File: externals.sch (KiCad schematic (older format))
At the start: 40 parts, among them J1 Micro_SD, J2 RC522_Header, J3 Screw_Terminal_1x02, P1 SWD, P2 VolDown, P3 Prev, P4 Play, P5 Next, P6 VolUp, P7 CONN_02X10, Q1 BSS138

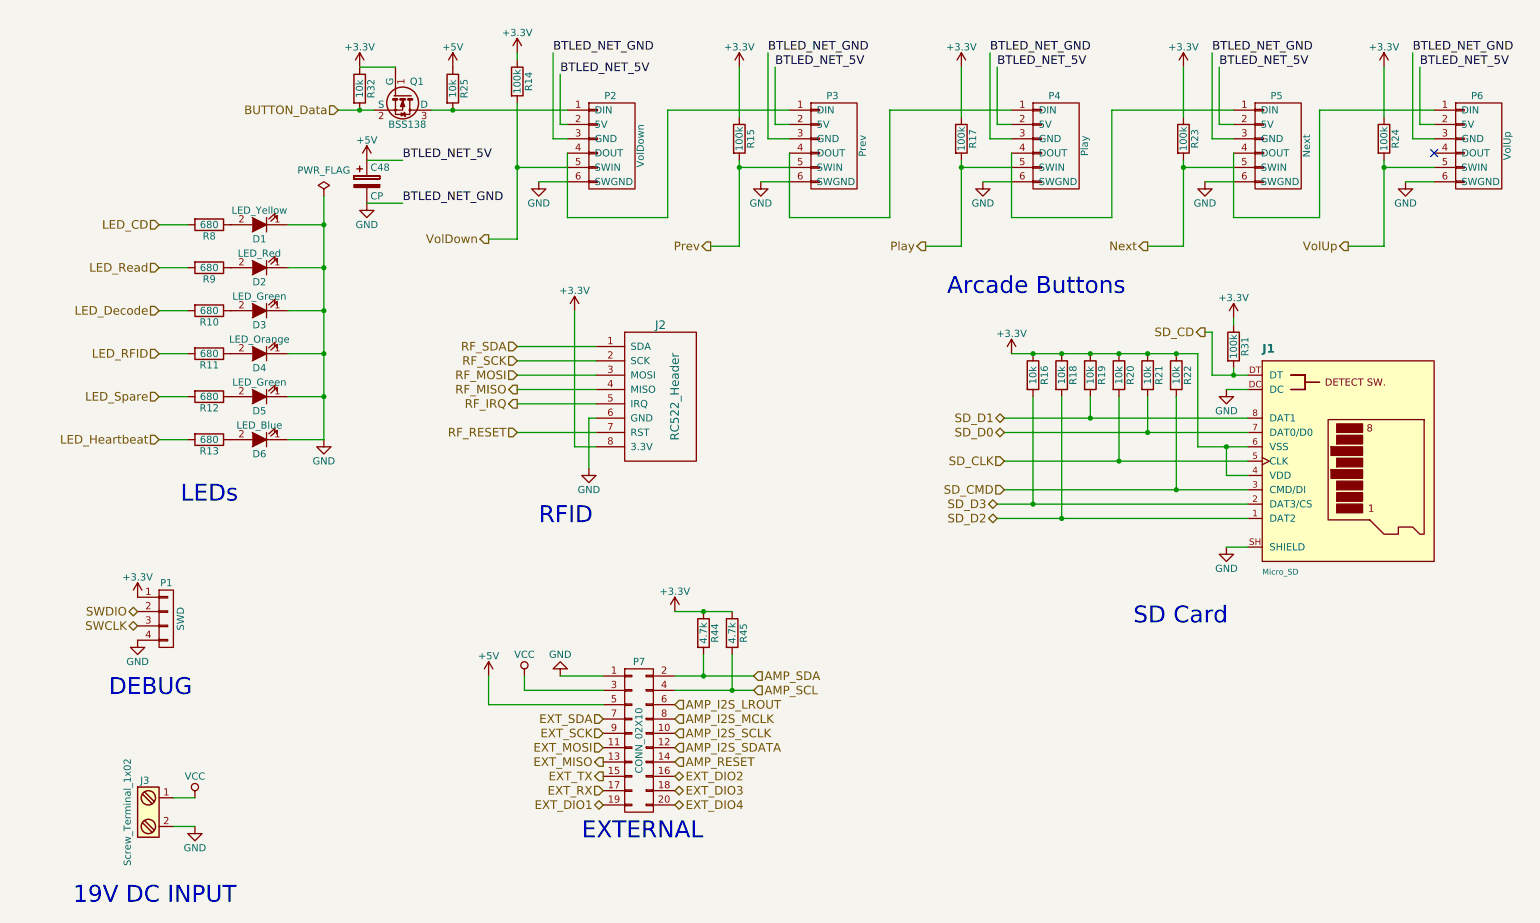
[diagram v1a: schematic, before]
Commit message: Use smd oscilator Add testpoints Use different power networks
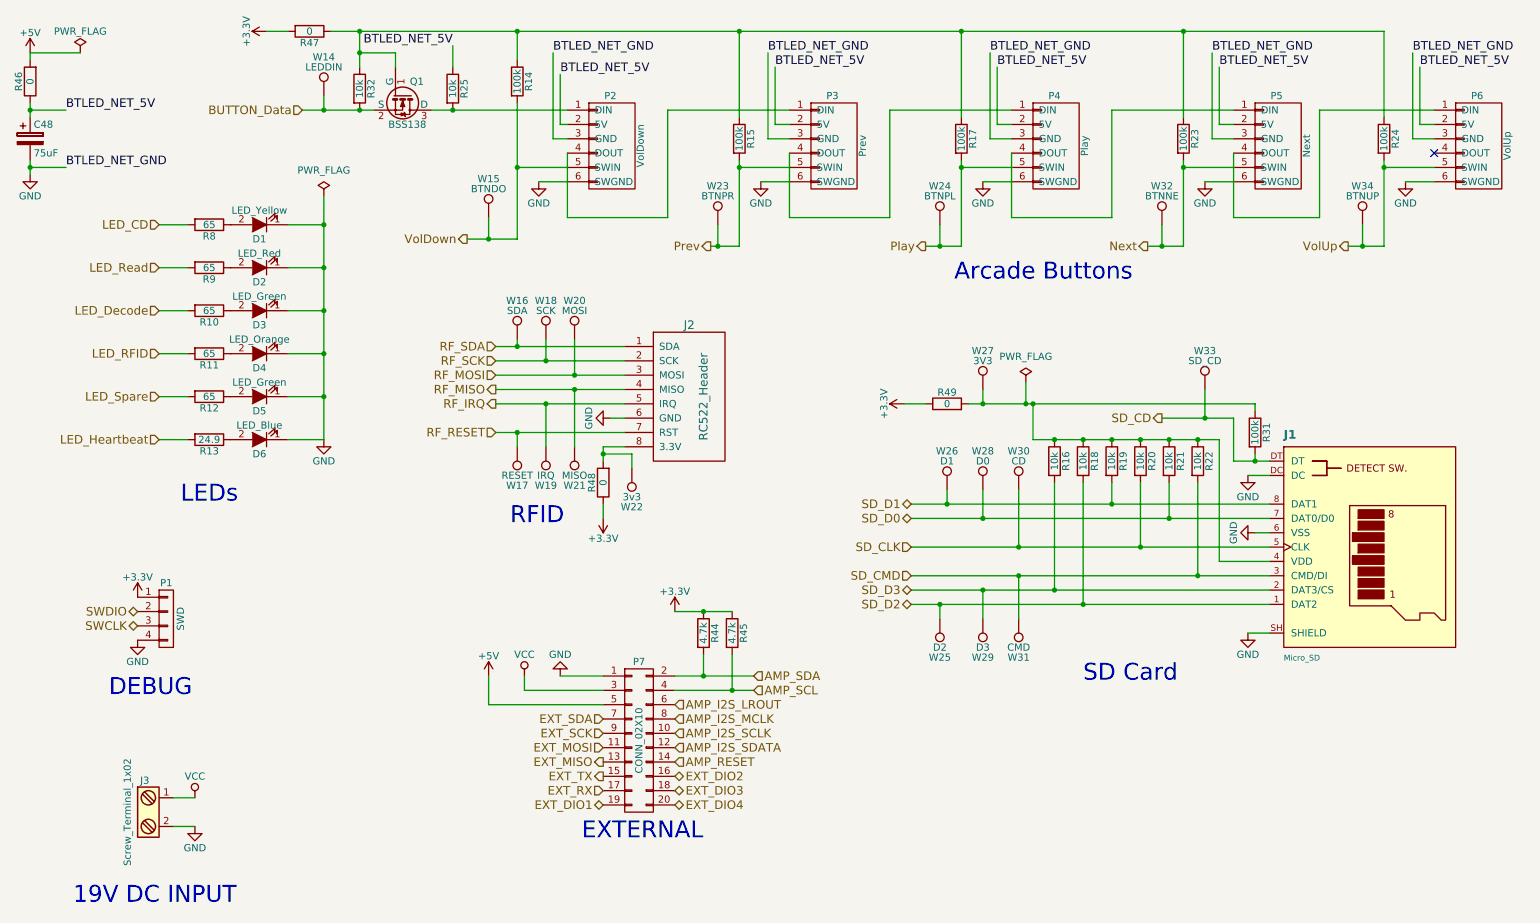
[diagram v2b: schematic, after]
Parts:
- added R46, R47: 0, Resistors_SMD:R_0603_HandSoldering, symbol R
- added R48, R49: 0, Resistors_SMD:R_0603, symbol R
- added W14: LEDDIN, Measurement_Points:Measurement_Point_Round-SMD-Pad_Small, symbol TEST_1P
- added W15: BTNDO, Measurement_Points:Measurement_Point_Round-SMD-Pad_Small, symbol TEST_1P
- added W16: SDA, Measurement_Points:Measurement_Point_Round-SMD-Pad_Small, symbol TEST_1P
- added W17: RESET, Measurement_Points:Measurement_Point_Round-SMD-Pad_Small, symbol TEST_1P
- added W18: SCK, Measurement_Points:Measurement_Point_Round-SMD-Pad_Small, symbol TEST_1P
- added W19: IRQ, Measurement_Points:Measurement_Point_Round-SMD-Pad_Small, symbol TEST_1P
- added W20: MOSI, Measurement_Points:Measurement_Point_Round-SMD-Pad_Small, symbol TEST_1P
- added W21: MISO, Measurement_Points:Measurement_Point_Round-SMD-Pad_Small, symbol TEST_1P
- added W22: 3v3, Measurement_Points:Measurement_Point_Round-SMD-Pad_Small, symbol TEST_1P
- added W23: BTNPR, Measurement_Points:Measurement_Point_Round-SMD-Pad_Small, symbol TEST_1P
- added W24: BTNPL, Measurement_Points:Measurement_Point_Round-SMD-Pad_Small, symbol TEST_1P
- added W25: D2, Measurement_Points:Measurement_Point_Round-SMD-Pad_Small, symbol TEST_1P
- added W26: D1, Measurement_Points:Measurement_Point_Round-SMD-Pad_Small, symbol TEST_1P
- added W27: 3V3, Measurement_Points:Measurement_Point_Round-SMD-Pad_Small, symbol TEST_1P
- added W28: D0, Measurement_Points:Measurement_Point_Round-SMD-Pad_Small, symbol TEST_1P
- added W29: D3, Measurement_Points:Measurement_Point_Round-SMD-Pad_Small, symbol TEST_1P
- added W30: CD, Measurement_Points:Measurement_Point_Round-SMD-Pad_Small, symbol TEST_1P
- added W31: CMD, Measurement_Points:Measurement_Point_Round-SMD-Pad_Small, symbol TEST_1P
- added W32: BTNNE, Measurement_Points:Measurement_Point_Round-SMD-Pad_Small, symbol TEST_1P
- added W33: SD_CD, Measurement_Points:Measurement_Point_Round-SMD-Pad_Small, symbol TEST_1P
- added W34: BTNUP, Measurement_Points:Measurement_Point_Round-SMD-Pad_Small, symbol TEST_1P
- C48: value CP -> 75uF; footprint Capacitors_THT:C_Radial_D5_L6_P2.5 -> Capacitors_SMD:c_elec_5x5.7
- R10, R11, R12, R8, R9: value 680 -> 65; MPN RC0603JR-07680RL -> RC0201FR-0764R9L; SPN 603-RC0603JR-07680RL -> 603-RC0201FR-0764R9L
- R13: value 680 -> 24.9; MPN RC0603JR-07680RL -> RC0201FR-0724R9L; SPN 603-RC0603JR-07680RL -> 603-RC0201FR-0724R9L
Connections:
- net +3V3: now also R47.2, R48.1, R49.1; no longer J1.4 (VDD), J1.6 (VSS), J2.8 (3.3V), Q1.1 (G), R14.1, R15.1, R16.1, R17.1, R18.1, R19.1, R20.1, R21.1, R22.1, R23.1, R24.1, R31.1, R32.1
- net +5V: now also R46.2; no longer C48.1, P2.2 (5V), P3.2 (5V), P4.2 (5V), P5.2 (5V), P6.2 (5V), R25.1
- net BUTTON_Data: now also W14.1
- net GND: now also J1.6 (VSS)
- net Next: now also W32.1
- net Play: now also W24.1
- net Prev: now also W23.1
- net RF_IRQ: now also W19.1
- net RF_MISO: now also W21.1
- net RF_MOSI: now also W20.1
- net RF_RESET: now also W17.1
- net RF_SCK: now also W18.1
- net RF_SDA: now also W16.1
- net SD_CD: now also W33.1
- net SD_CLK: now also W30.1
- net SD_CMD: now also W31.1
- net SD_D0: now also W28.1
- net SD_D1: now also W26.1
- net SD_D2: now also W25.1
- net SD_D3: now also W29.1
- net VolDown: now also W15.1
- net VolUp: now also W34.1
- new net: Q1.1 (G), R14.1, R15.1, R17.1, R23.1, R24.1, R32.1, R47.1
- new net: J1.4 (VDD), R16.1, R18.1, R19.1, R20.1, R21.1, R22.1, R31.1, R49.2, W27.1
- new net: J2.8 (3.3V), R48.2, W22.1
- new net BTLED_NET_5V: C48.1, P2.2 (5V), P3.2 (5V), P4.2 (5V), P5.2 (5V), P6.2 (5V), R25.1, R46.1
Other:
- moved on the sheet: C48, J1, J2, R16, R18, R19, R20, R21, R22, R31

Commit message: new layout
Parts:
- D1, D2, D3, D4, D5, D6: footprint Capacitors_SMD:C_0603_HandSoldering -> Diodes_SMD:D_0603
- R10, R11, R12, R8, R9: value 65 -> 680; footprint Resistors_SMD:R_0603_HandSoldering -> Resistors_SMD:R_0603; MPN RC0201FR-0764R9L -> RC0603JR-07680RL; SPN 603-RC0201FR-0764R9L -> 603-RC0603JR-07680RL
- R13: value 24.9 -> 680; footprint Resistors_SMD:R_0603_HandSoldering -> Resistors_SMD:R_0603; MPN RC0201FR-0724R9L -> RC0603JR-07680RL; SPN 603-RC0201FR-0724R9L -> 603-RC0603JR-07680RL
- R14, R15, R16, R17, R18, R19, R20, R21, R22, R23, R24, R25, R31, R32, R44, R45, R46, R47: footprint Resistors_SMD:R_0603_HandSoldering -> Resistors_SMD:R_0603

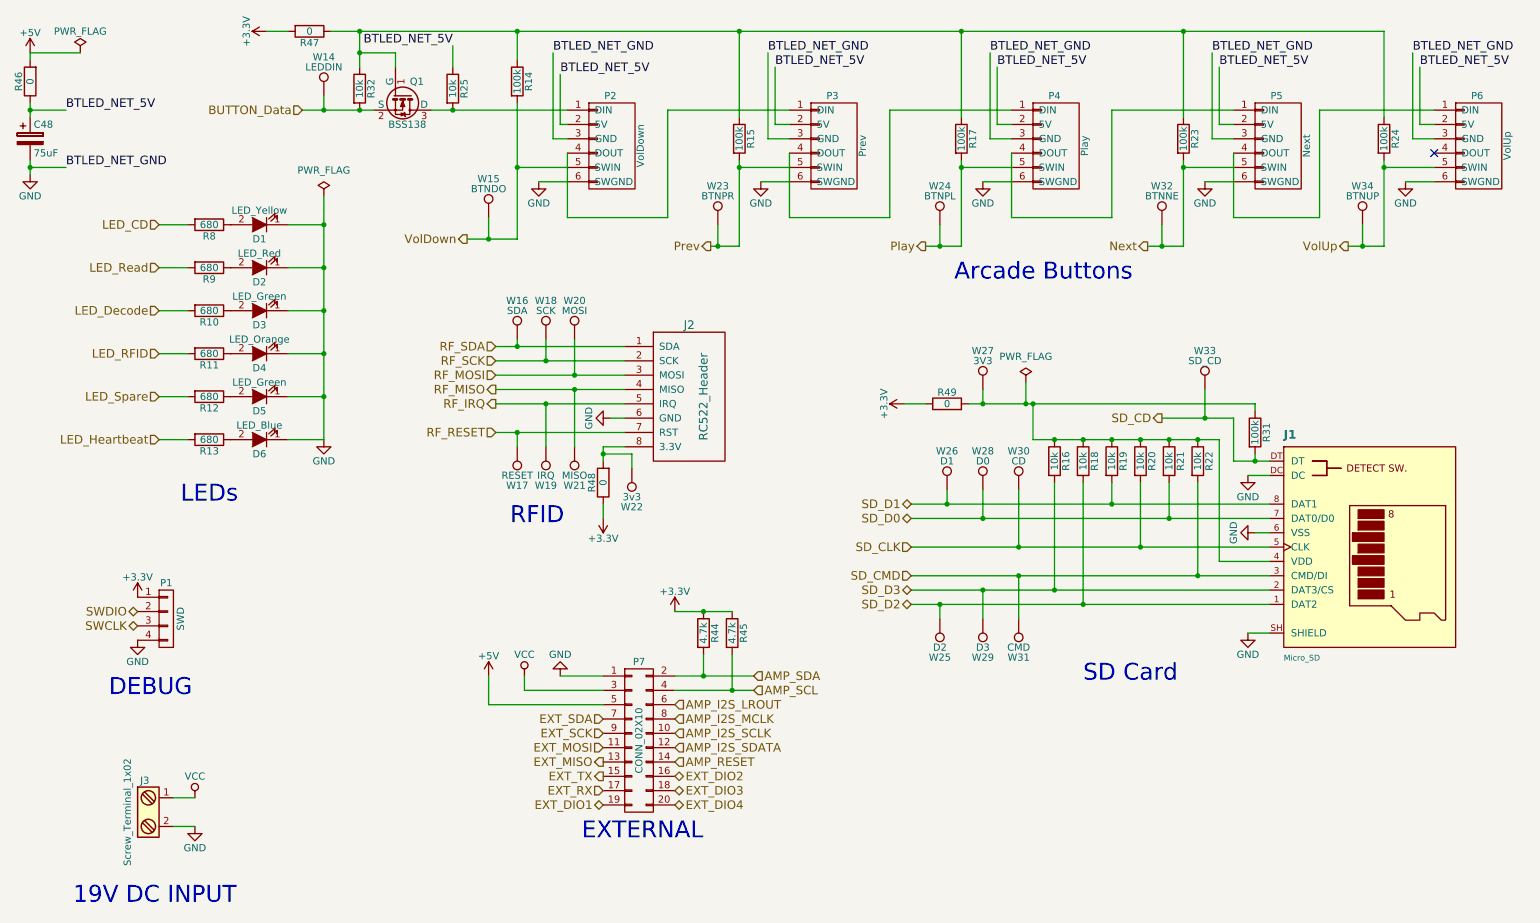
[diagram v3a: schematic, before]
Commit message: Macrofab sd card footprint
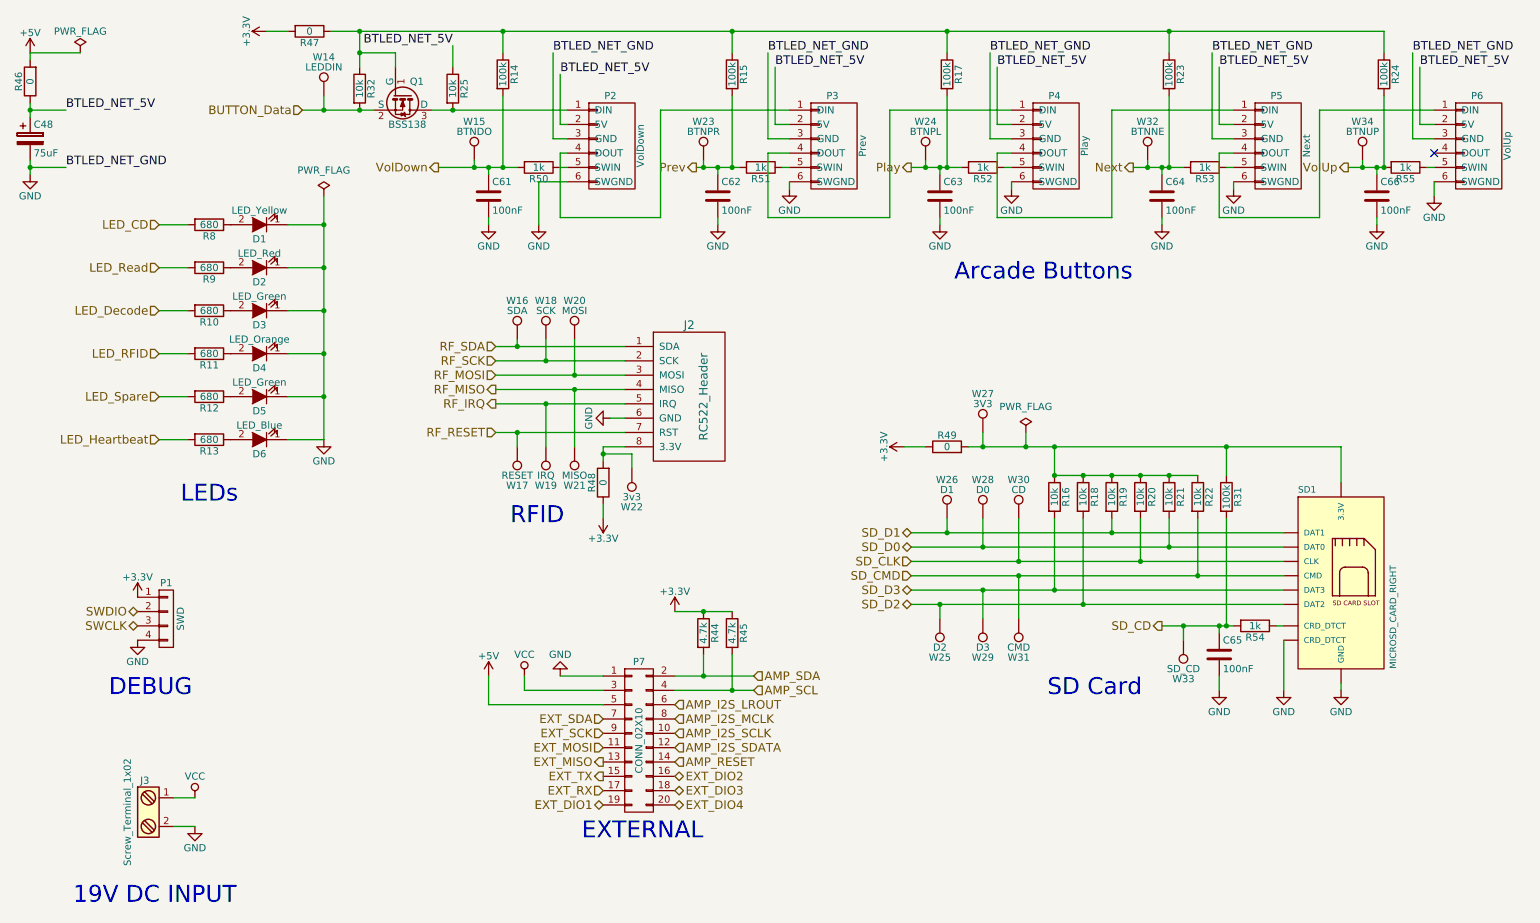
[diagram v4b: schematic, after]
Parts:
- removed J1: Micro_SD, conn-io:HIROSE-MICROSD-DM3AT-SF, symbol Micro_SD
- added C61, C62, C63, C64, C65, C66: 100nF, Capacitors_SMD:C_0402, symbol C
- added R50, R51, R52, R53, R54, R55: 1k, Resistors_SMD:R_0603, symbol R
- added SD1: MICROSD_CARD_RIGHT, MF_Connectors_MF-MICROSD, symbol MICROSD_CARD_RIGHT
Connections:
- net GND: now also C61.2, C62.2, C63.2, C64.2, C65.2, C66.2, SD1.10 (CRD_DTCT), SD1.6 (GND), SD1.G0 (GND), SD1.G1 (GND)
- net Next: now also C64.1, R53.2; no longer P5.5 (SWIN)
- net Play: now also C63.1, R52.2; no longer P4.5 (SWIN)
- net Prev: now also C62.1, R51.2; no longer P3.5 (SWIN)
- net SD_CD: now also C65.1, R54.2
- net SD_CLK: now also SD1.5 (CLK)
- net SD_CMD: now also SD1.3 (CMD)
- net SD_D0: now also SD1.7 (DAT0)
- net SD_D1: now also SD1.8 (DAT1)
- net SD_D2: now also SD1.1 (DAT2)
- net SD_D3: now also SD1.2 (DAT3)
- net VolDown: now also C61.1, R50.2; no longer P2.5 (SWIN)
- net VolUp: now also C66.1, R55.2; no longer P6.5 (SWIN)
- net at R16.1, R18.1, R19.1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: now also SD1.4 (3.3V)
- new net: P2.5 (SWIN), R50.1
- new net: P3.5 (SWIN), R51.1
- new net: P4.5 (SWIN), R52.1
- new net: P5.5 (SWIN), R53.1
- new net: P6.5 (SWIN), R55.1
- new net: R54.1, SD1.9 (CRD_DTCT)
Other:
- moved on the sheet: R14, R15, R16, R17, R18, R19, R20, R21, R22, R23, R24, R31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

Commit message: Finished new layout
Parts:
- C48: MFR (none) -> Panasonic; MPN (none) -> EEE-HD1V100AR; SPN (none) -> 667-EEE-HD1V100AR; SPR (none) -> Mouser
- C61, C62, C63, C64, C65, C66: MFR (none) -> KEMET; MPN (none) -> C0402C104M4RACAUTO; SPN (none) -> 80-C0402C104M4RAUTO; SPR (none) -> Mouser
- R46, R47: MPN RC0603JR-07100KL -> RC0603JR-070RL; SPN 603-RC0603JR-07100KL -> 603-RC0603JR-070RL
- SD1: MFR (none) -> Molex; MPN (none) -> 47334-0001; SPN (none) -> 538-47334-0001; SPR (none) -> Mouser
- W22: value 3v3 -> 3V3

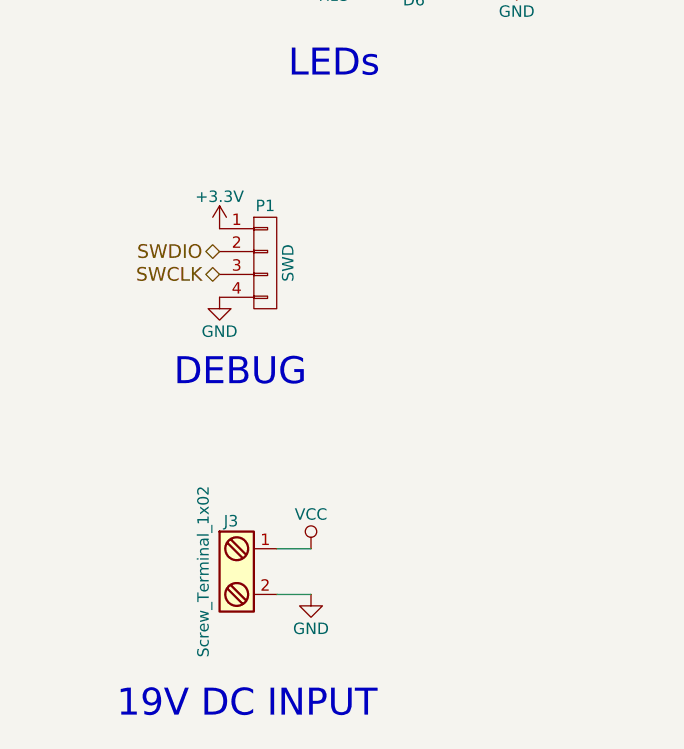
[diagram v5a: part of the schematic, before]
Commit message: Remove 3. LDO some improvements
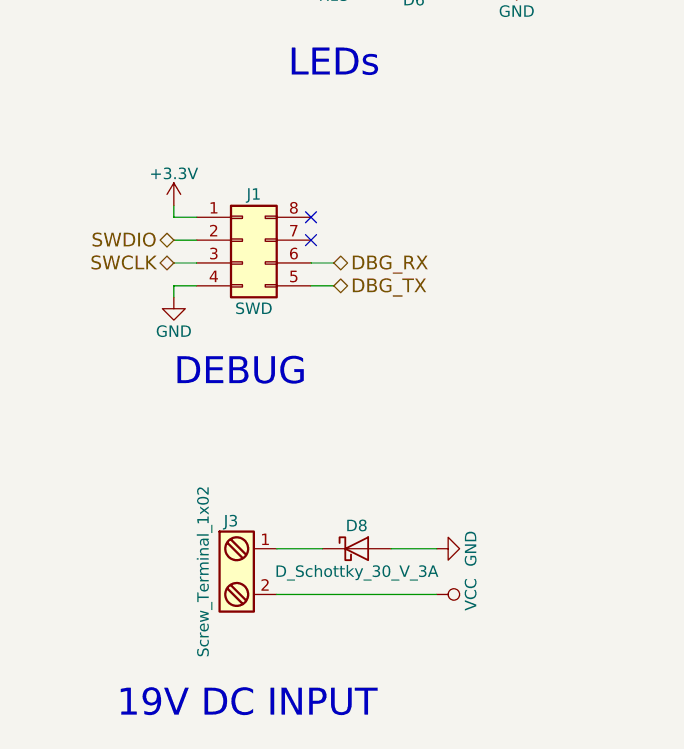
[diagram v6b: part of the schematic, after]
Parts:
- removed P1: SWD, Pin_Headers:Pin_Header_Straight_1x04, symbol CONN_01X04
- added D8: D_Schottky_30_V_3A, Diodes_SMD:SMB_Standard, symbol D_Schottky
- added J1: SWD, Pin_Headers:Pin_Header_Straight_2x04, symbol Conn_02x04_Counter_Clockwise
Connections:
- net +3V3: now also J1.1 (Pin_1)
- net GND: now also D8.2 (A), J1.4 (Pin_4); no longer J3.2
- net SWCLK: now also J1.3 (Pin_3)
- net SWDIO: now also J1.2 (Pin_2)
- net VCC: now also J3.2; no longer J3.1
- new net: D8.1 (K), J3.1
- new net DBG_RX: J1.6 (Pin_6)
- new net DBG_TX: J1.5 (Pin_5)
- no-connect marks 1 -> 3
